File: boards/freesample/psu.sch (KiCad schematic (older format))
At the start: 162 parts, among them U26 MCP1755ST-5002E/MC, U27 LM27761, U28 ADP1763Z-1.0, U29 ADP1763Z-1.0, U30 OKL-T/3-W12P-C, U31 ADP1741, U32 OKL-T/3-W12P-C, U33 ADP1741, U34 ADP1741, U35 OKL-T/3-W12P-C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

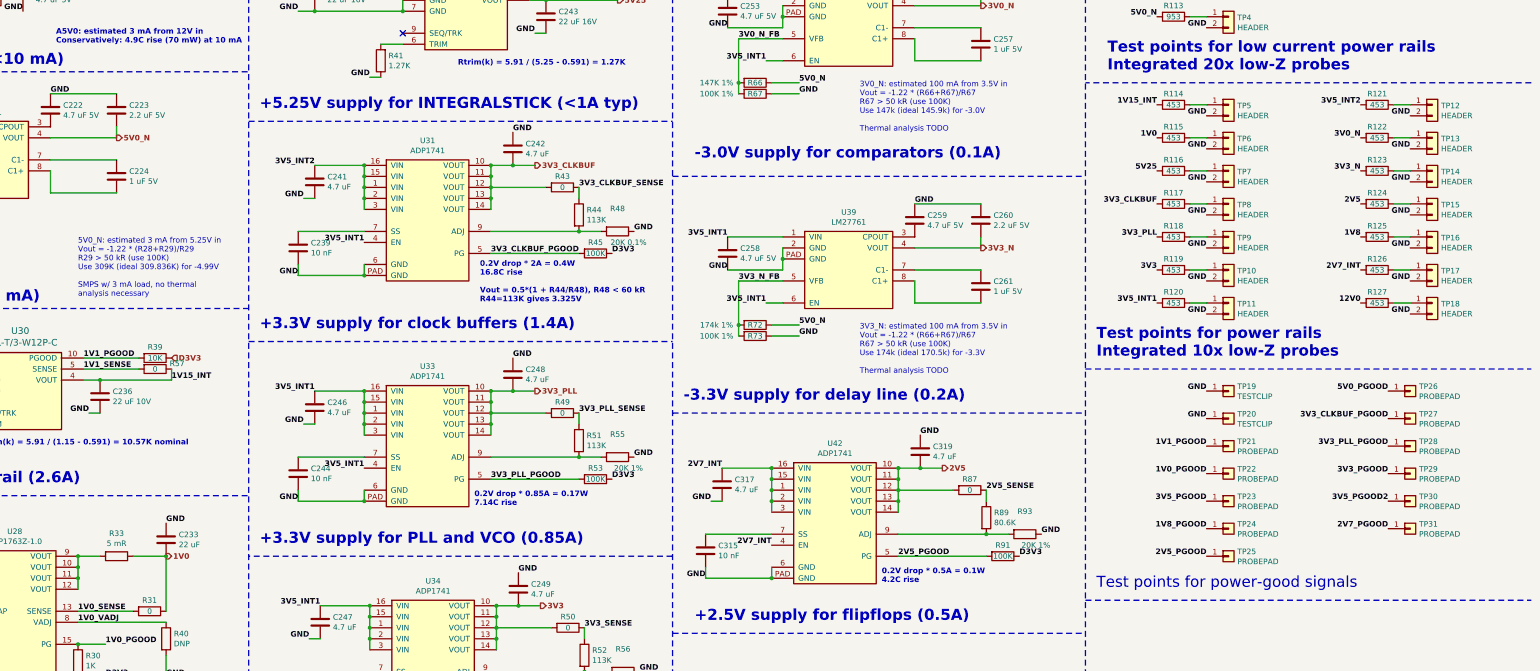
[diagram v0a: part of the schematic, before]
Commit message: Added fiducials
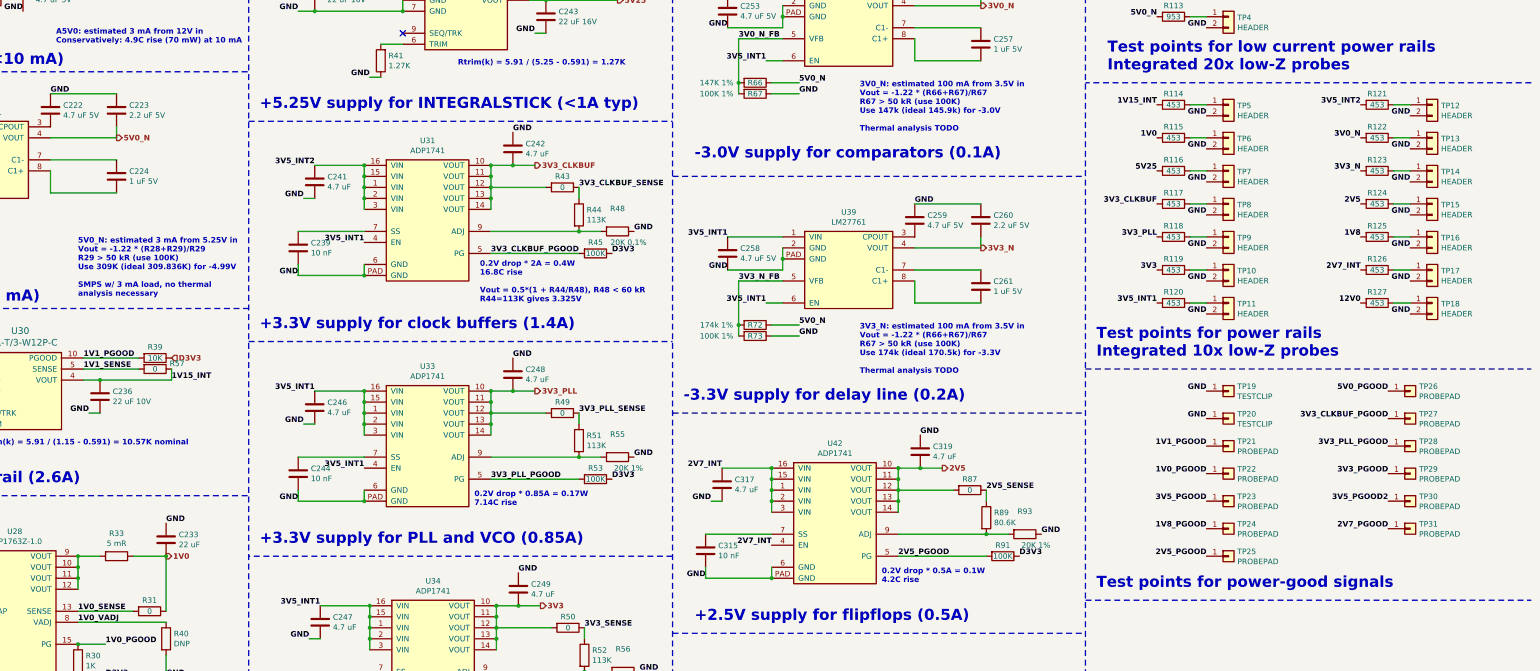
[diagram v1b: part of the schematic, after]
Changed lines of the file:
@@
 Wire Wire Line
 	1550 3100 1300 3100
-Text Notes 2850 3750 0    50   ~ 0
+Text Notes 2850 3750 0    50   ~ 6
 5V0_N: estimated 3 mA from 5.25V in\nVout = -1.22 * (R28+R29)/R29\nR29 > 50 kR (use 100K)\nUse 309K (ideal 309.836K) for -4.99V\n\nSMPS w/ 3 mA load, no thermal\nanalysis necessary
 Text Notes 1200 9700 0    50   ~ 6
@@
 Wire Wire Line
 	9400 1900 9150 1900
-Text Notes 9950 2250 0    50   ~ 0
+Text Notes 9950 2250 0    50   ~ 6
 3V0_N: estimated 100 mA from 3.5V in\nVout = -1.22 * (R66+R67)/R67\nR67 > 50 kR (use 100K)\nUse 147k (ideal 145.9k) for -3.0V\n\nThermal analysis TODO
 Text Label 8750 3200 2    50   ~ 6
@@
 Wire Wire Line
 	9400 4100 9150 4100
-Text Notes 9950 4450 0    50   ~ 0
+Text Notes 9950 4450 0    50   ~ 6
 3V3_N: estimated 100 mA from 3.5V in\nVout = -1.22 * (R66+R67)/R67\nR67 > 50 kR (use 100K)\nUse 174k (ideal 170.5k) for -3.3V\n\nThermal analysis TODO
 Wire Notes Line width 20 style solid
@@
 	1    0    0    -1
 $EndComp
-Text Notes 12100 6400 0    100  ~ 0
+Text Notes 12100 6400 0    100  ~ 6
 Test points for power-good signals
 Wire Notes Line width 20 style solid
